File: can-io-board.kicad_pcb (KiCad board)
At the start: 2 copper layers, 15 x 22.5 mm, 21 parts, among them P1 CONN_01X08, P2 CONN_01X08, U1 STM32F302K8U6, U2 MCP1703, U3 MAX3051, X1 XTAL-SMD-4-PADS

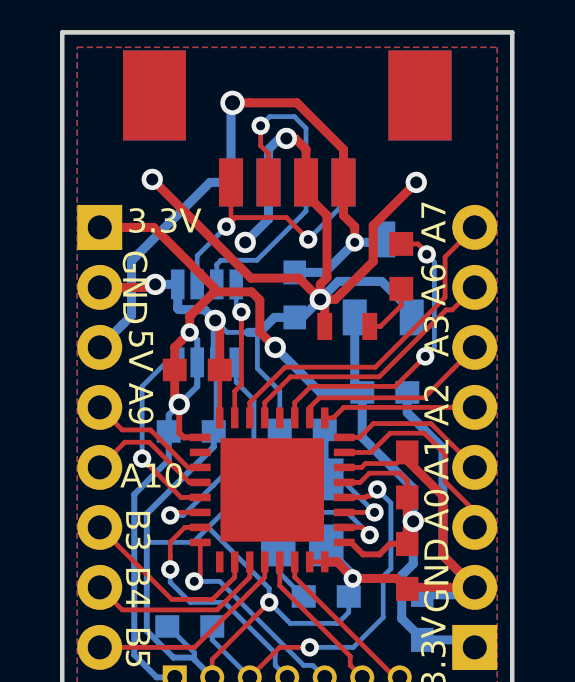
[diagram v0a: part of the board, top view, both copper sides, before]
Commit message: optimize C9 connection
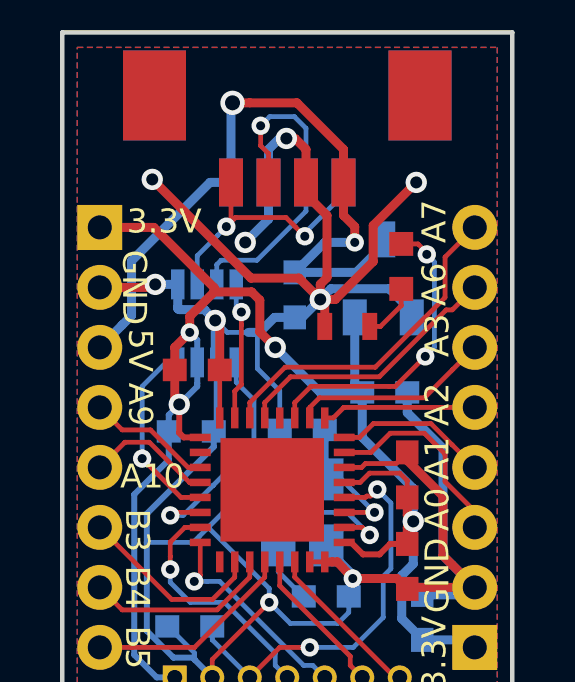
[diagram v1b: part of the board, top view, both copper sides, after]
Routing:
- net /5V_CAN: track 21.4 -> 24.1 mm
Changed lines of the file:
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@@
     (thickness 1.6)
     (drawings 25)
-    (tracks 379)
+    (tracks 383)
     (zones 0)
     (modules 21)
@@
   )
   (setup
-    (last_trace_width 0.16)
+    (last_trace_width 0.3)
     (user_trace_width 0.2)
     (user_trace_width 0.3)
@@
       (drillshape 0)
       (scaleselection 1)
-      (outputdirectory ""))
+      (outputdirectory gerber/))
   )
   (net 0 "")
@@
     (effects (font (size 0.8 0.8) (thickness 0.2)))
   )
-  (gr_text A10 (at 90.5 54.8 360) (layer F.SilkS)
+  (gr_text A10 (at 90.5 54.8) (layer F.SilkS)
     (effects (font (size 0.8 0.8) (thickness 0.2)))
   )
@@
     (effects (font (size 0.8 0.8) (thickness 0.2)))
   )
-  (gr_text 3.3V (at 90.9 46.3 360) (layer F.SilkS)
+  (gr_text 3.3V (at 90.9 46.3) (layer F.SilkS)
     (effects (font (size 0.8 0.8) (thickness 0.2)))
   )
@@
   (segment (start 99 54.94) (end 98.750482 54.690482) (width 0.16) (layer F.Cu) (net 1))
   (segment (start 98.750482 54.690482) (end 97.740141 54.690482) (width 0.16) (layer F.Cu) (net 1))
+  (segment (start 96.454999 48.545001) (end 96.1 48.9) (width 0.3) (layer B.Cu) (net 2))
+  (segment (start 98.395001 48.545001) (end 96.454999 48.545001) (width 0.3) (layer B.Cu) (net 2))
+  (segment (start 99.15 49.3) (end 98.395001 48.545001) (width 0.3) (layer B.Cu) (net 2))
+  (segment (start 99.15 49.5) (end 99.15 49.3) (width 0.3) (layer B.Cu) (net 2))
   (segment (start 101.25 58.5) (end 99.05 58.5) (width 0.3) (layer F.Cu) (net 2))
   (segment (start 99.05 58.5) (end 99 58.55) (width 0.3) (layer F.Cu) (net 2))
@@
   (segment (start 96.325 48.172955) (end 96.1 48.397955) (width 0.3) (layer F.Cu) (net 2))
   (segment (start 96.1 48.397955) (end 96.1 48.9) (width 0.3) (layer F.Cu) (net 2))
-  (segment (start 98.15 48.3) (end 96.7 48.3) (width 0.3) (layer B.Cu) (net 2))
-  (segment (start 96.7 48.3) (end 96.1 48.9) (width 0.3) (layer B.Cu) (net 2))
-  (segment (start 99.15 49.3) (end 98.15 48.3) (width 0.3) (layer B.Cu) (net 2))
-  (segment (start 99.15 49.3) (end 99.15 49.5) (width 0.3) (layer B.Cu) (net 2))
   (segment (start 96.25 49.8) (end 96.25 49.05) (width 0.3) (layer F.Cu) (net 2))
   (segment (start 96.25 49.05) (end 96.1 48.9) (width 0.3) (layer F.Cu) (net 2))
@@
   (segment (start 97.496291 56.5) (end 97.749348 56.753057) (width 0.16) (layer F.Cu) (net 5))
   (via (at 97.749348 56.753057) (size 0.61) (drill 0.3) (layers F.Cu B.Cu) (net 5))
+  (segment (start 97.3 48) (end 98.2 47.1) (width 0.3) (layer B.Cu) (net 6))
+  (segment (start 95.25 48) (end 97.3 48) (width 0.3) (layer B.Cu) (net 6))
+  (segment (start 98.2 47.1) (end 98.2 46.9) (width 0.3) (layer B.Cu) (net 6))
+  (segment (start 96.25 47) (end 95.25 48) (width 0.3) (layer B.Cu) (net 6))
+  (segment (start 97.25 47) (end 96.25 47) (width 0.3) (layer B.Cu) (net 6))
   (segment (start 93.125 42.398572) (end 93.175859 42.347713) (width 0.3) (layer B.Cu) (net 6))
   (segment (start 96.875 43.8998) (end 95.322913 42.347713) (width 0.3) (layer F.Cu) (net 6))
@@
   (segment (start 89.810001 49.439999) (end 89.499999 49.750001) (width 0.3) (layer B.Cu) (net 6))
   (segment (start 89.499999 49.750001) (end 88.75 50.5) (width 0.3) (layer B.Cu) (net 6))
-  (segment (start 97.25 47) (end 96.25 48) (width 0.3) (layer B.Cu) (net 6))
-  (segment (start 96.25 48) (end 95.25 48) (width 0.3) (layer B.Cu) (net 6))
-  (segment (start 97.25 47) (end 98.1 47) (width 0.3) (layer B.Cu) (net 6))
   (segment (start 98.1 47) (end 98.2 46.9) (width 0.3) (layer B.Cu) (net 6))
   (segment (start 97.25 46.4748) (end 97.25 47) (width 0.3) (layer F.Cu) (net 6))
@@
   (segment (start 94.375 44.0398) (end 94.11336 43.77816) (width 0.16) (layer F.Cu) (net 9))
   (segment (start 94.11336 43.77816) (end 94.11336 43.111454) (width 0.16) (layer F.Cu) (net 9))
-  (segment (start 95.7 46.9) (end 96.875 45.725) (width 0.16) (layer B.Cu) (net 10))
-  (segment (start 96.875 45.725) (end 96.875 44.9998) (width 0.16) (layer B.Cu) (net 10))
+  (segment (start 94.958959 46.170042) (end 95.279575 46.490658) (width 0.16) (layer F.Cu) (net 10))
+  (segment (start 95.279575 46.490658) (end 95.584574 46.795657) (width 0.16) (layer F.Cu) (net 10))
   (segment (start 92.970049 46.475041) (end 93.275048 46.170042) (width 0.16) (layer F.Cu) (net 10))
-  (segment (start 93.275048 46.170042) (end 94.970042 46.170042) (width 0.16) (layer F.Cu) (net 10))
-  (segment (start 94.970042 46.170042) (end 95.7 46.9) (width 0.16) (layer F.Cu) (net 10))
-  (via (at 95.7 46.9) (size 0.61) (drill 0.3) (layers F.Cu B.Cu) (net 10))
+  (segment (start 95.584574 46.690226) (end 95.584574 46.795657) (width 0.16) (layer B.Cu) (net 10))
+  (segment (start 93.275048 46.170042) (end 94.958959 46.170042) (width 0.16) (layer F.Cu) (net 10))
+  (segment (start 96.875 45.3998) (end 95.584574 46.690226) (width 0.16) (layer B.Cu) (net 10))
+  (segment (start 96.875 44.9998) (end 96.875 45.3998) (width 0.16) (layer B.Cu) (net 10))
+  (via (at 95.584574 46.795657) (size 0.61) (drill 0.3) (layers F.Cu B.Cu) (net 10))
   (segment (start 92 48.4) (end 92 47.44509) (width 0.16) (layer B.Cu) (net 10))
   (segment (start 93.125 44.9998) (end 93.125 46.32009) (width 0.16) (layer F.Cu) (net 10))

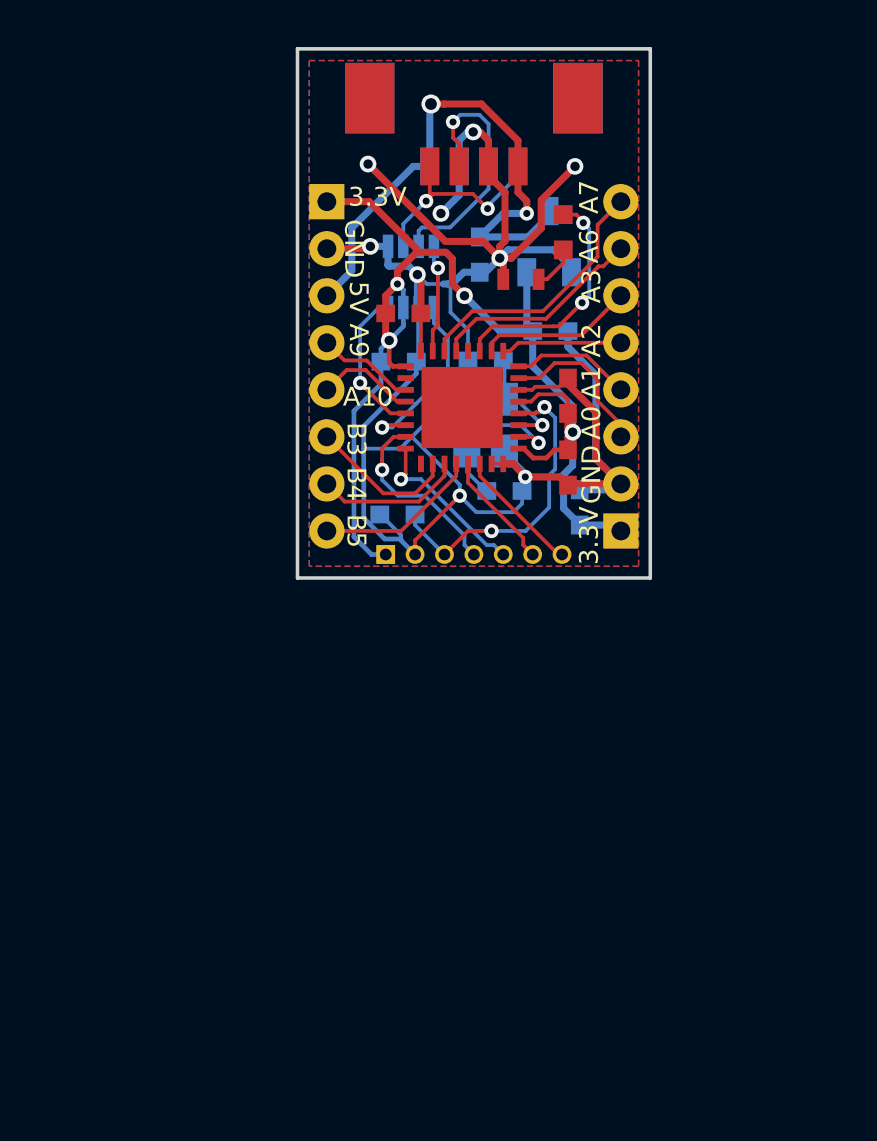
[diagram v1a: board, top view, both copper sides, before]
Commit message: Start layout on RevB
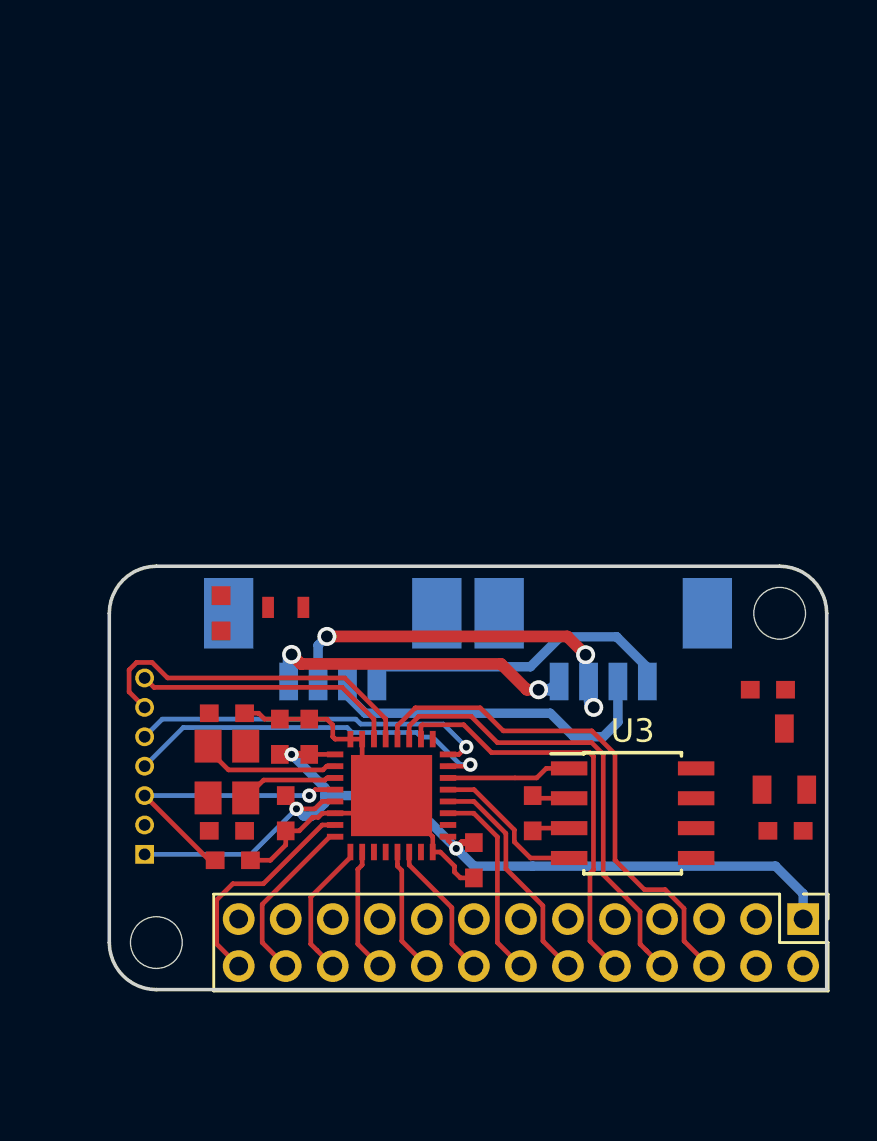
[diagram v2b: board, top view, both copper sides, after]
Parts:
- removed P1, P2: CONN_01X08, _connectors:_Pin2mm_8
- added G***: LOGO, _logo:CVRA-logo-small, B.Cu at (107.7, 69.3)
- added H1: MountingHole M2, MountingHole:MountingHole_2.2mm_M2_DIN965, F.Cu at (81.5, 78.0)
- added H2: MountingHole M2, MountingHole:MountingHole_2.2mm_M2_DIN965, F.Cu at (108.0, 64.0)
- added J1: Conn_02x13_Odd_Even, Connector_PinHeader_2.00mm:PinHeader_2x13_P2.00mm_Vertical, F.Cu at (109.0, 77.0)
- C1, C10, C4, C6, C7, C8, C9, U2: moved to F.Cu
- CONN3: moved to B.Cu
- U3: footprint _std:_SOT23-8 -> Package_SO:SOIC-8_3.9x4.9mm_P1.27mm; moved to F.Cu
- X1: value XTAL-SMD-4-PADS -> 16MHz 10ppm; moved to F.Cu
- moved C10 23.5 mm to (108.2, 73.2), turned to 180 degrees
- moved U2 23.4 mm to (107.2, 71.5), turned to 0 degrees
- moved C2 23.4 mm to (95.0, 74.5), turned to 270 degrees
- moved U3 23.1 mm to (101.8, 72.5), turned to 0 degrees
- moved C6 22.8 mm to (84.5, 73.2)
- moved CONN2 22.7 mm to (89.0, 64.0)
- moved CONN3 22.6 mm to (100.5, 64.0), turned to 0 degrees
- moved C9 22.2 mm to (107.5, 67.2), turned to 180 degrees
- moved D1 21.8 mm to (84.2, 64.0), turned to 270 degrees
- moved C3 21.4 mm to (87.0, 72.5), turned to 270 degrees
- moved C8 20.0 mm to (97.5, 72.5), turned to 90 degrees
- moved X1 18.4 mm to (84.5, 70.8), turned to 90 degrees
- moved R1 17.2 mm to (87.0, 63.8), turned to 0 degrees
- moved U1 16.8 mm to (91.5, 71.8), turned to 0 degrees
- moved CONN1 16.4 mm to (81.0, 74.2), turned to 90 degrees
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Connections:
- U1 pad 12: Net-(U1-Pad12) -> (no net)
- U1 pad 15: /CAN_EN -> (no net)
- U1 pad 18: Net-(U1-Pad18) -> (no net)
- U1 pad 25: Net-(U1-Pad25) -> (no net)
- U1 pad 33: (no net) -> GND
- U3 pad 8: /CAN_EN -> GND
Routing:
- net GND: track 103.1 -> 35.4 mm, vias 9 -> 3
- net /IO_PB5_SPI3MOSI: track 6.98 -> 22.1 mm
- net /IO_PB4_SPI3MISO_UART2RX: track 6.27 -> 19.7 mm
- net /IO_PB3_SPI3SCK_UART2TX: track 6.31 -> 17.9 mm
- net /5V_CAN: track 24.1 -> 13.4 mm
- net /LED: track 10.2 -> 0.00 mm, vias 2 -> 0
- net /IO_PB6_I2C1SCL_UART1TX: track 4.99 -> 14.8 mm
- net VCC: track 52.2 -> 43.3 mm, vias 4 -> 3
- net /SWCK: track 7.06 -> 15.4 mm
- net /SWIO: track 8.00 -> 16.2 mm
- net /IO_PB7_I2C1SDA_UART1RX: track 5.39 -> 11.3 mm
- net /IO_PA10_I2C2SDA_UART1RX: track 4.25 -> 9.76 mm
- net /IO_PA7_TIM17CH1_ADC15: track 11.2 -> 5.99 mm
- net /CAN_EN: track 4.61 -> 0.00 mm, vias 1 -> 0
- net Net-(CONN2-Pad4): track 9.20 -> 13.7 mm, vias 2 -> 0
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- removed copper zone on B.Cu, net GND
- removed copper zone on F.Cu, net GND
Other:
- board size 15 x 22.5 mm -> 30.5 x 18 mm
- board text added: "CAN-IO RevB"
- board text added: "CVRA"
- board text removed: "+"
- board text removed: "CAN-IO RevA"

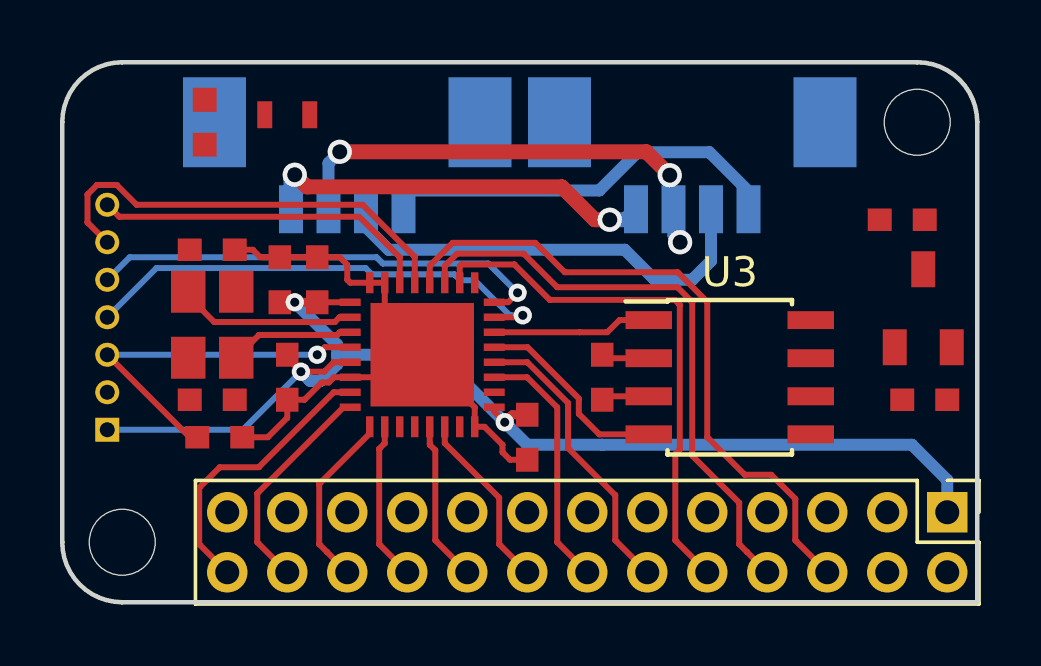
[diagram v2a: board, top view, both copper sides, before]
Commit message: CAN connector on opposite sides
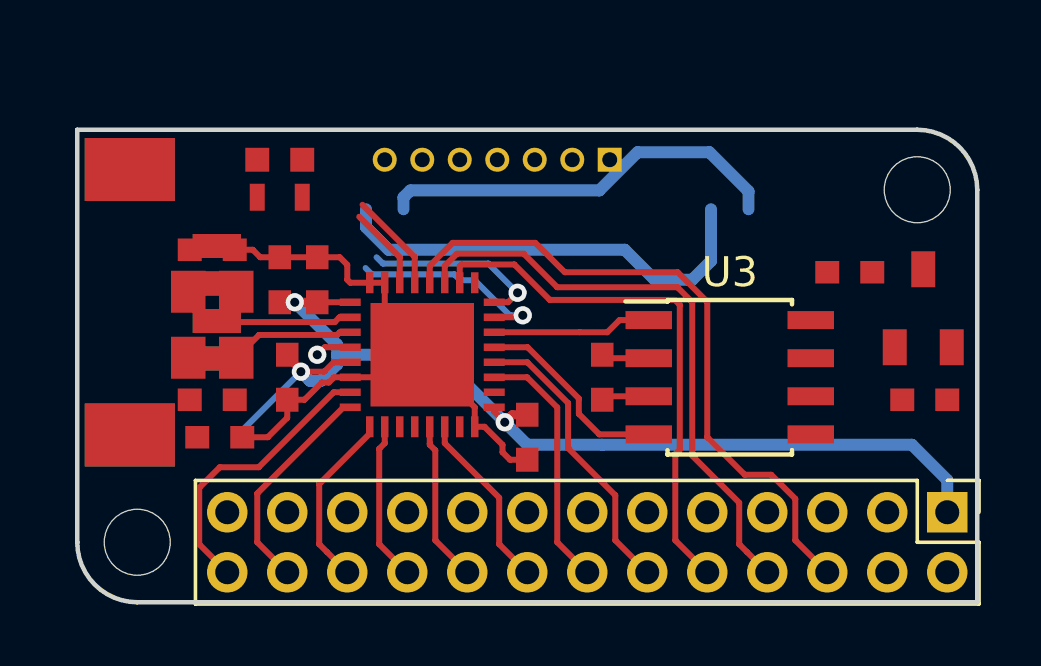
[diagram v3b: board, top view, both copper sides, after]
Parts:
- CONN2: moved to F.Cu
- moved CONN3 19.7 mm to (81.8, 70.0), turned to 90 degrees
- moved CONN1 19.0 mm to (97.8, 65.2), turned to 180 degrees
- moved CONN2 9.41 mm to (81.8, 70.0), turned to 270 degrees
- moved D1 2.79 mm to (86.8, 65.2), turned to 0 degrees
- moved R1 2.76 mm to (86.8, 66.5)
- moved C9 2.47 mm to (105.8, 69.0)
- moved H2 2.25 mm to (108.0, 66.2)
- moved H1 0.50 mm to (82.0, 78.0)
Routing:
- net GND: track 35.4 -> 19.7 mm, vias 3 -> 0
- net /5V_CAN: track 13.4 -> 0.00 mm, vias 2 -> 0
- net /IO_PB6_I2C1SCL_UART1TX: track 14.8 -> 3.32 mm
- net /RST: track 12.3 -> 1.20 mm
- net /SWIO: track 16.2 -> 6.87 mm
- net /SWCK: track 15.4 -> 6.10 mm
- net /IO_PB7_I2C1SDA_UART1RX: track 11.3 -> 2.76 mm
- net VCC: track 43.3 -> 38.8 mm
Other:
- board size 30.5 x 18 mm -> 30 x 15.8 mm
